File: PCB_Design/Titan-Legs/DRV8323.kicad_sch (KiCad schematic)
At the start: 26 parts, among them IC3 DRV8323RSRGZT, J2 691214110003, Q1 BSC031N06NS3GATMA1, Q2 BSC031N06NS3GATMA1, Q3 BSC031N06NS3GATMA1, Q4 BSC031N06NS3GATMA1, Q5 BSC031N06NS3GATMA1, Q6 BSC031N06NS3GATMA1

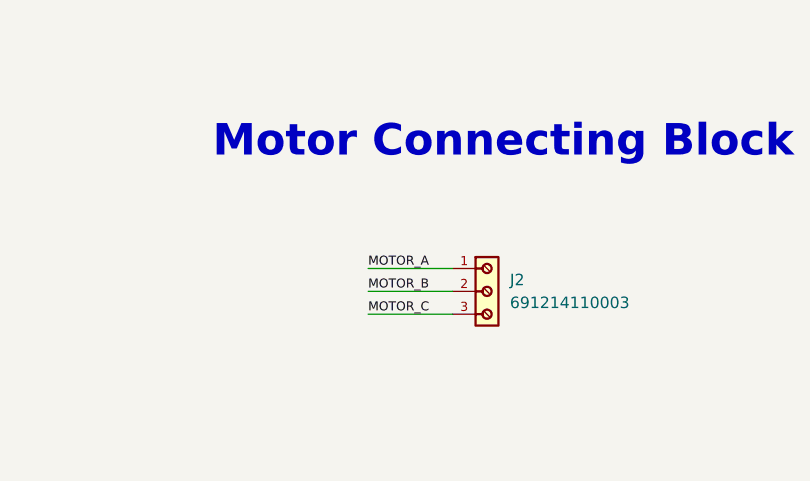
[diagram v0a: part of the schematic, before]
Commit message: Add new placement for Quadruped PCB
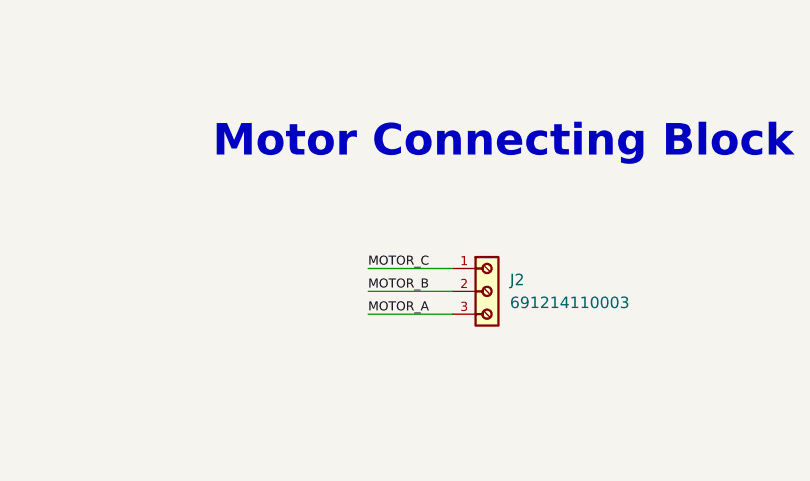
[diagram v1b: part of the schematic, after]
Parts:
- IC3: footprint KiCad:QFN50P700X700X100-49N-D -> DRV8323RS:QFN50P700X700X100-49N-D
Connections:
- net MOTOR_A: now also J2.3; no longer J2.1
- net MOTOR_C: now also J2.1; no longer J2.3
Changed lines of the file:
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@@
     (effects (font (size 1 1)) (justify right bottom))
   )
-  (label "MOTOR_C" (at 55.372 181.61 0)
+  (label "MOTOR_A" (at 55.372 181.61 0)
     (effects (font (size 1 1)) (justify left bottom))
   )
@@
     (effects (font (size 1 1)) (justify right bottom))
   )
-  (label "MOTOR_A" (at 55.372 176.53 0)
+  (label "MOTOR_C" (at 55.372 176.53 0)
     (effects (font (size 1 1)) (justify left bottom))
   )
@@
     (property "Reference" "IC3" (id 0) (at 218.059 65.659 0))
     (property "Value" "DRV8323RSRGZT" (id 1) (at 218.059 68.199 0))
-    (property "Footprint" "KiCad:QFN50P700X700X100-49N-D" (id 2) (at 209.804 56.134 0)
-      (effects (font (size 1.27 1.27)) (justify left) hide)
-    )
+    (property "Footprint" "DRV8323RS:QFN50P700X700X100-49N-D" (id 2) (at 209.804 56.134 0)
+      (effects (font (size 1.27 1.27)) (justify left) hide)
+    )

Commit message: Added high voltage copper fills
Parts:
- D5: footprint LED_SMD:LED_0603_1608Metric -> LED_SMD:LED_0402_1005Metric
- R17, R18: footprint Resistor_SMD:R_0603_1608Metric -> Resistor_SMD:R_0402_1005Metric
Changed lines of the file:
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@@
       (effects (font (size 0.762 0.762)) (justify right))
     )
-    (property "Footprint" "LED_SMD:LED_0603_1608Metric" (id 2) (at 249.5296 88.9508 0)
+    (property "Footprint" "LED_SMD:LED_0402_1005Metric" (id 2) (at 249.5296 88.9508 0)
       (effects (font (size 1.27 1.27)) hide)
     )
@@
       (effects (font (size 0.762 0.762)) (justify left))
     )
-    (property "Footprint" "Resistor_SMD:R_0603_1608Metric" (id 2) (at 254.1016 90.2208 90)
+    (property "Footprint" "Resistor_SMD:R_0402_1005Metric" (id 2) (at 254.1016 90.2208 90)
       (effects (font (size 1.27 1.27)) hide)
     )
@@
       (effects (font (size 0.762 0.762)) (justify left))
     )
-    (property "Footprint" "Resistor_SMD:R_0603_1608Metric" (id 2) (at 247.7516 97.3328 90)
-      (effects (font (size 1.27 1.27)) hide)
-    )
+    (property "Footprint" "Resistor_SMD:R_0402_1005Metric" (id 2) (at 247.7516 97.3328 90)
+      (effects (font (size 1.27 1.27)) hide)
+    )

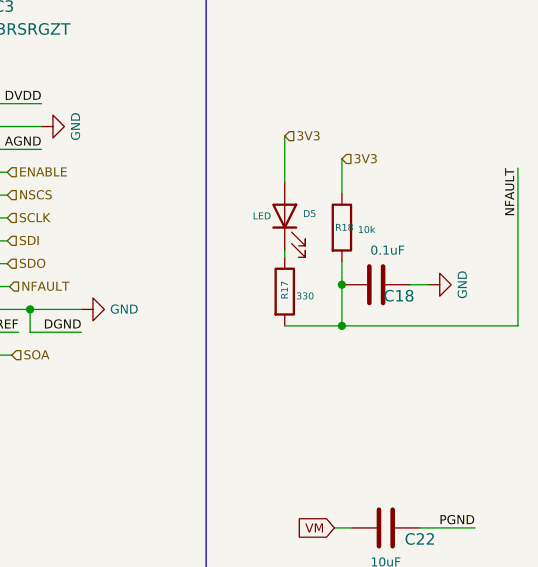
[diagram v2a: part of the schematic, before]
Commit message: Merged the silkscreen MA,MB,MC and added vias in shunt resistors
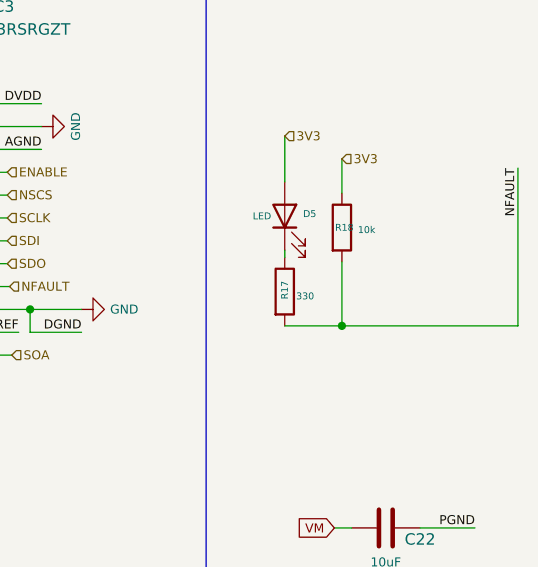
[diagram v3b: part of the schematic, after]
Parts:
- removed C18: 0.1uF, Capacitor_SMD:C_0603_1608Metric, symbol Device:C
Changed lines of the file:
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@@
   (junction (at 217.424 78.994) (diameter 0) (color 0 0 0 0)
-  )
-  (junction (at 255.8796 96.5708) (diameter 0) (color 0 0 0 0)
   )
   (junction (at 30.48 71.12) (diameter 0) (color 0 0 0 0)
@@
     (stroke (width 0) (type default) (color 0 0 0 0))
   )
-  (wire (pts (xy 255.8796 96.5708) (xy 255.8796 101.1428))
-    (stroke (width 0) (type default) (color 0 0 0 0))
-  )
   (wire (pts (xy 256.9464 123.5964) (xy 255.0414 123.5964))
     (stroke (width 0) (type default) (color 0 0 0 0))
@@
     (stroke (width 0) (type default) (color 0 0 0 0))
   )
-  (wire (pts (xy 265.4808 96.5708) (xy 263.4996 96.5708))
-    (stroke (width 0) (type default) (color 0 0 0 0))
-  )
   (wire (pts (xy 83.82 45.72) (xy 83.82 41.91))
     (stroke (width 0) (type default) (color 0 0 0 0))
@@
     (stroke (width 0) (type default) (color 0 0 0 0))
   )
-  (wire (pts (xy 255.8796 94.0308) (xy 255.8796 96.5708))
+  (wire (pts (xy 255.8796 94.0308) (xy 255.8796 101.1428))
     (stroke (width 0) (type default) (color 0 0 0 0))
   )
@@
     (pin "1")
     (pin "2")
-  )
-  (symbol (lib_id "power:GND") (at 265.4808 96.5708 90) (unit 1)
-    (in_bom yes) (on_board yes)
-    (property "Reference" "#PWR038" (id 0) (at 271.8308 96.5708 0)
-      (effects (font (size 1.27 1.27)) hide)
-    )
-    (property "Value" "GND" (id 1) (at 269.2908 96.5708 0)
-      (effects (font (size 1 1)))
-    )
-    (property "Footprint" "" (id 2) (at 265.4808 96.5708 0)
-      (effects (font (size 1.27 1.27)) hide)
-    )
-    (property "Datasheet" "" (id 3) (at 265.4808 96.5708 0)
-      (effects (font (size 1.27 1.27)) hide)
-    )
-    (pin "1")
   )
   (symbol (lib_id "Device:R") (at 27.94 111.76 0) (unit 1)
@@
     (pin "1")
   )
-  (symbol (lib_id "Device:C") (at 259.6896 96.5708 90) (unit 1)
-    (in_bom yes) (on_board yes)
-    (property "Reference" "C18" (id 0) (at 262.2296 97.8408 90))
-    (property "Value" "0.1uF" (id 1) (at 260.9596 92.7608 90)
-      (effects (font (size 1 1)))
-    )
-    (property "Footprint" "Capacitor_SMD:C_0603_1608Metric" (id 2) (at 263.4996 95.6056 0)
-      (effects (font (size 1.27 1.27)) hide)
-    )
-    (property "Datasheet" "~" (id 3) (at 259.6896 96.5708 0)
-      (effects (font (size 1.27 1.27)) hide)
-    )
-    (pin "1")
-    (pin "2")
-  )
   (symbol (lib_id "Device:R") (at 255.8796 90.2208 0) (unit 1)
